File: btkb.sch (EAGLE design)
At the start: 1 part

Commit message: I added the RN-42 to the schematic! lol!
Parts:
- removed JP1: (no value), jumper:JP4E
- added U$1: BLUETOOTH-RN41", SparkFun-RF:BLUETOOTH-RN41"
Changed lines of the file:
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@@
 <layer number="48" name="Document" color="7" fill="1" visible="no" active="no"/>
 <layer number="49" name="Reference" color="7" fill="1" visible="no" active="no"/>
+<layer number="50" name="dxf" color="7" fill="1" visible="no" active="no"/>
 <layer number="51" name="tDocu" color="7" fill="1" visible="no" active="no"/>
 <layer number="52" name="bDocu" color="7" fill="1" visible="no" active="no"/>
+<layer number="53" name="tGND_GNDA" color="7" fill="9" visible="no" active="no"/>
+<layer number="54" name="bGND_GNDA" color="1" fill="9" visible="no" active="no"/>
+<layer number="56" name="wert" color="7" fill="1" visible="no" active="no"/>
+<layer number="57" name="tCAD" color="7" fill="1" visible="no" active="no"/>
 <layer number="90" name="Modules" color="5" fill="1" visible="yes" active="yes"/>
 <layer number="91" name="Nets" color="2" fill="1" visible="yes" active="yes"/>
@@
 <layer number="97" name="Info" color="7" fill="1" visible="yes" active="yes"/>
 <layer number="98" name="Guide" color="6" fill="1" visible="yes" active="yes"/>
+<layer number="99" name="SpiceOrder" color="7" fill="1" visible="no" active="no"/>
+<layer number="100" name="Muster" color="7" fill="1" visible="no" active="no"/>
+<layer number="101" name="Patch_Top" color="12" fill="4" visible="yes" active="yes"/>
+<layer number="102" name="Vscore" color="7" fill="1" visible="yes" active="yes"/>
+<layer number="103" name="tMap" color="7" fill="1" visible="yes" active="yes"/>
+<layer number="104" name="Name" color="16" fill="1" visible="yes" active="yes"/>
+<layer number="105" name="tPlate" color="7" fill="1" visible="yes" active="yes"/>
+<layer number="106" name="bPlate" color="7" fill="1" visible="yes" active="yes"/>
+<layer number="107" name="Crop" color="7" fill="1" visible="yes" active="yes"/>
+<layer number="108" name="tplace-old" color="10" fill="1" visible="yes" active="yes"/>
+<layer number="109" name="ref-old" color="11" fill="1" visible="yes" active="yes"/>
+<layer number="110" name="fp0" color="7" fill="1" visible="yes" active="yes"/>
+<layer number="111" name="LPC17xx" color="7" fill="1" visible="yes" active="yes"/>
+<layer number="112" name="tSilk" color="7" fill="1" visible="yes" active="yes"/>
+<layer number="113" name="IDFDebug" color="4" fill="1" visible="yes" active="yes"/>
+<layer number="116" name="Patch_BOT" color="9" fill="4" visible="yes" active="yes"/>
+<layer number="121" name="_tsilk" color="7" fill="1" visible="yes" active="yes"/>
+<layer number="122" name="_bsilk" color="7" fill="1" visible="yes" active="yes"/>
+<layer number="123" name="tTestmark" color="7" fill="1" visible="yes" active="yes"/>
+<layer number="124" name="bTestmark" color="7" fill="1" visible="yes" active="yes"/>
+<layer number="125" name="_tNames" color="7" fill="1" visible="yes" active="yes"/>
+<layer number="126" name="_bNames" color="7" fill="1" visible="yes" active="yes"/>
+<layer number="127" name="_tValues" color="7" fill="1" visible="yes" active="yes"/>
+<layer number="128" name="_bValues" color="7" fill="1" visible="yes" active="yes"/>
+<layer number="131" name="tAdjust" color="7" fill="1" visible="yes" active="yes"/>
+<layer number="132" name="bAdjust" color="7" fill="1" visible="yes" active="yes"/>
+<layer number="144" name="Drill_legend" color="7" fill="1" visible="yes" active="yes"/>
+<layer number="150" name="Notes" color="7" fill="1" visible="yes" active="yes"/>
+<layer number="151" name="HeatSink" color="7" fill="1" visible="yes" active="yes"/>
+<layer number="152" name="_bDocu" color="7" fill="1" visible="yes" active="yes"/>
+<layer number="153" name="FabDoc1" color="7" fill="1" visible="yes" active="yes"/>
+<layer number="154" name="FabDoc2" color="7" fill="1" visible="yes" active="yes"/>
+<layer number="155" name="FabDoc3" color="7" fill="1" visible="yes" active="yes"/>
+<layer number="199" name="Contour" color="7" fill="1" visible="yes" active="yes"/>
+<layer number="200" name="200bmp" color="1" fill="10" visible="yes" active="yes"/>
+<layer number="201" name="201bmp" color="2" fill="10" visible="yes" active="yes"/>
+<layer number="202" name="202bmp" color="3" fill="10" visible="yes" active="yes"/>
+<layer number="203" name="203bmp" color="4" fill="10" visible="yes" active="yes"/>
+<layer number="204" name="204bmp" color="5" fill="10" visible="yes" active="yes"/>
+<layer number="205" name="205bmp" color="6" fill="10" visible="yes" active="yes"/>
+<layer number="206" name="206bmp" color="7" fill="10" visible="yes" active="yes"/>
+<layer number="207" name="207bmp" color="8" fill="10" visible="yes" active="yes"/>
+<layer number="208" name="208bmp" color="9" fill="10" visible="yes" active="yes"/>
+<layer number="209" name="209bmp" color="7" fill="1" visible="yes" active="yes"/>
+<layer number="210" name="210bmp" color="7" fill="1" visible="yes" active="yes"/>
+<layer number="211" name="211bmp" color="7" fill="1" visible="yes" active="yes"/>
+<layer number="212" name="212bmp" color="7" fill="1" visible="yes" active="yes"/>
+<layer number="213" name="213bmp" color="7" fill="1" visible="yes" active="yes"/>
+<layer number="214" name="214bmp" color="7" fill="1" visible="yes" active="yes"/>
+<layer number="215" name="215bmp" color="7" fill="1" visible="yes" active="yes"/>
+<layer number="216" name="216bmp" color="7" fill="1" visible="yes" active="yes"/>
+<layer number="217" name="217bmp" color="18" fill="1" visible="no" active="no"/>
+<layer number="218" name="218bmp" color="19" fill="1" visible="no" active="no"/>
+<layer number="219" name="219bmp" color="20" fill="1" visible="no" active="no"/>
+<layer number="220" name="220bmp" color="21" fill="1" visible="no" active="no"/>
+<layer number="221" name="221bmp" color="22" fill="1" visible="no" active="no"/>
+<layer number="222" name="222bmp" color="23" fill="1" visible="no" active="no"/>
+<layer number="223" name="223bmp" color="24" fill="1" visible="no" active="no"/>
+<layer number="224" name="224bmp" color="25" fill="1" visible="no" active="no"/>
+<layer number="248" name="Housing" color="7" fill="1" visible="yes" active="yes"/>
+<layer number="249" name="Edge" color="7" fill="1" visible="yes" active="yes"/>
+<layer number="250" name="Descript" color="3" fill="1" visible="no" active="no"/>
+<layer number="251" name="SMDround" color="12" fill="11" visible="no" active="no"/>
+<layer number="254" name="cooling" color="7" fill="1" visible="yes" active="yes"/>
 </layers>
 <schematic xreflabel="%F%N/%S.%C%R" xrefpart="/%S.%C%R">
@@
 </classes>
 <parts>
-<part name="JP1" library="jumper" deviceset="JP4E" device=""/>
+<part name="U$1" library="SparkFun-RF" deviceset="BLUETOOTH-RN41" device="&quot;"/>
 </parts>
 <sheets>
@@
 </plain>
 <instances>
-<instance part="JP1" gate="G$1" x="20.32" y="93.98"/>
+<instance part="U$1" gate="G$1" x="73.66" y="12.7"/>
 </instances>
 <busses>

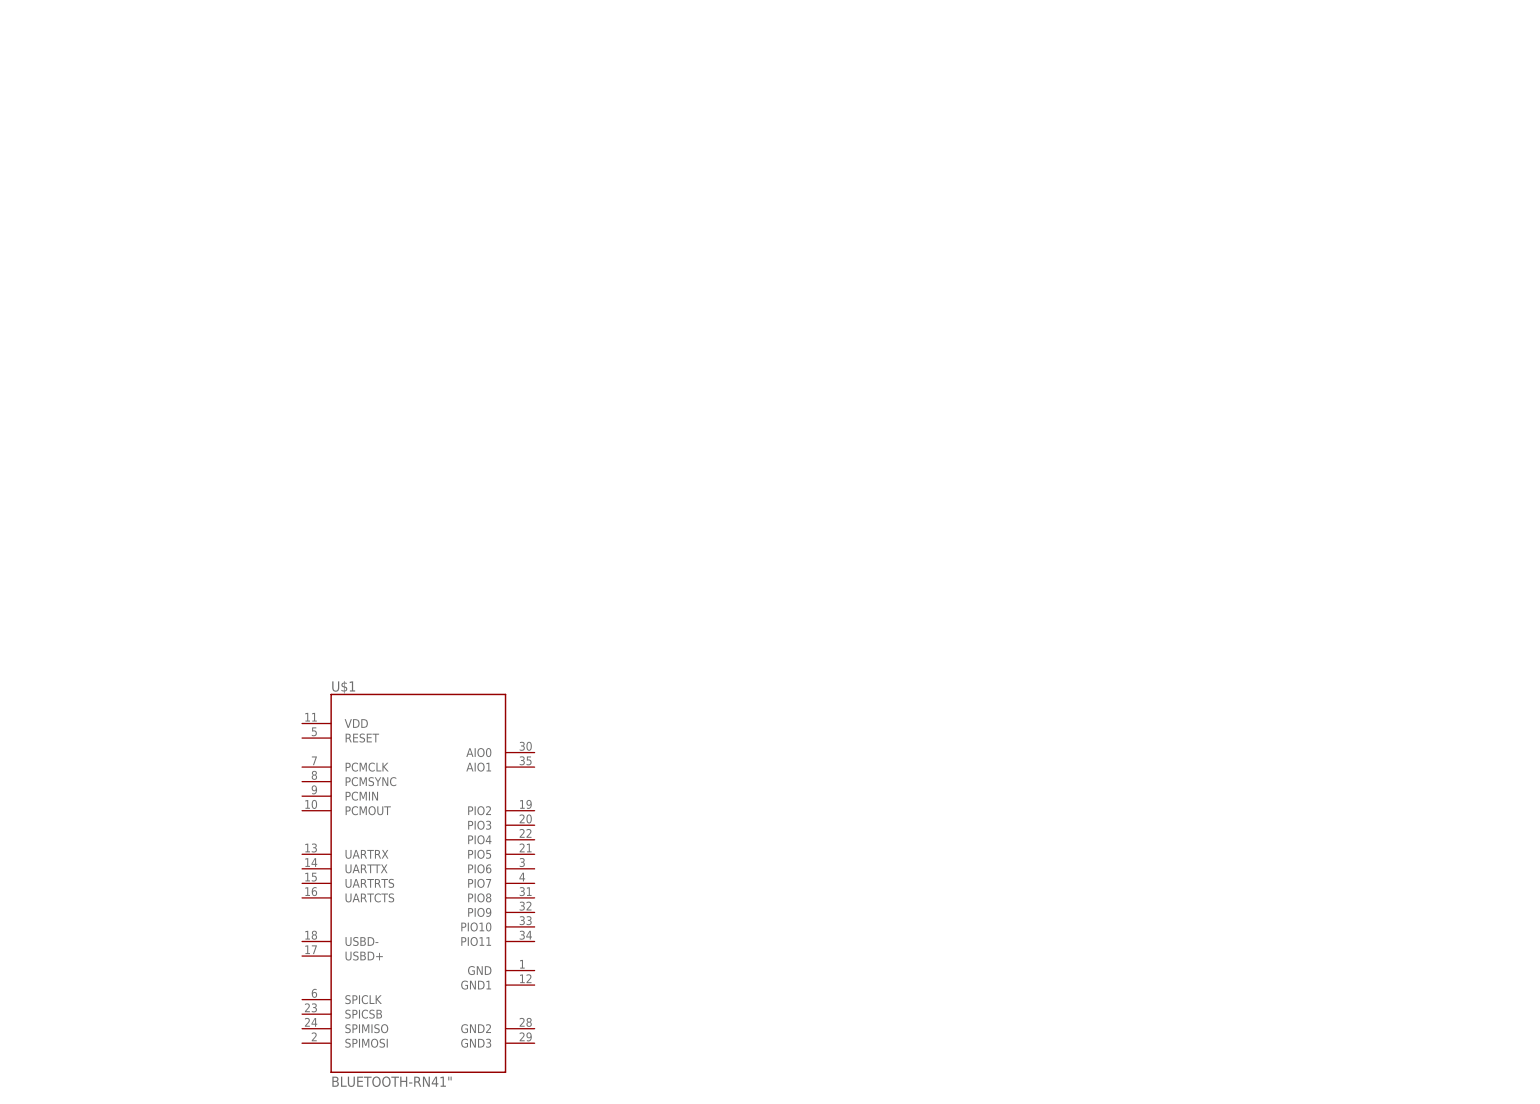
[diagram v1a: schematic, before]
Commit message: Added components copy pasta'ed from other schematics
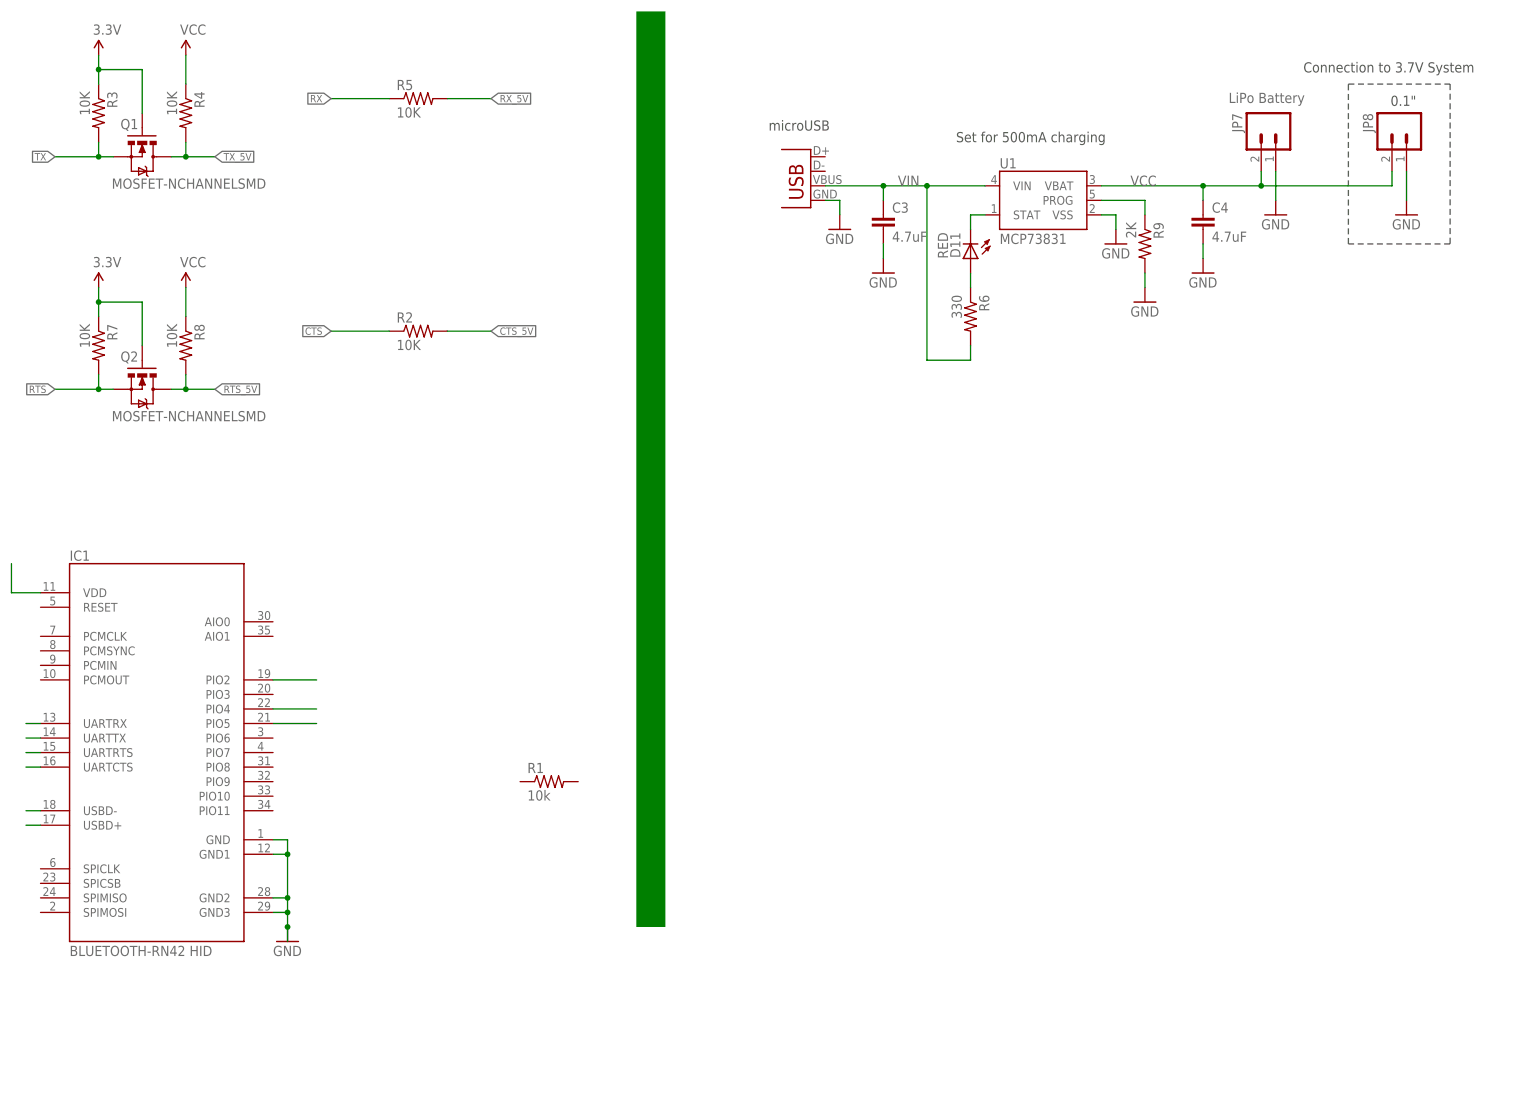
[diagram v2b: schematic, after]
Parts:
- removed U$1: BLUETOOTH-RN41", SparkFun-RF:BLUETOOTH-RN41"
- added C3, C4: 4.7uF, SparkFun:CAP0402-CAP
- added D11: RED, SparkFun:LED0603
- added IC1: BLUETOOTH-RN42 HID, SparkFun-RF:BLUETOOTH-RN41"
- added JP7: LiPo Battery, SparkFun:M02-JST-2MM-SMT
- added JP8: (no value), SparkFun:M02PTH
- added Q1, Q2: MOSFET-NCHANNELSMD, SparkFun:MOSFET-NCHANNELSMD
- added R1: 10k, SparkFun-Resistors:0.22OHM-1/4W-1%(0805)
- added R2, R3, R4, R5, R7, R8: 10K, SparkFun:RESISTOR0603-RES
- added R6: 330, SparkFun:RESISTOR0402-RES
- added R9: 2K, SparkFun:RESISTOR0402-RES
- added U1: MCP73831, SparkFun:MCP73831
- added X1: Micro USB, SparkFun:USB-MICROB
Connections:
- new net 3.3V: Q1.G, Q2.G, R3.1, R7.1
- new net CTS: R2.1
- new net CTS_5V: R2.2
- new net GND: C3.2, C4.2, IC1.GND, IC1.GND1, IC1.GND2, IC1.GND3, JP7.1, JP8.1, R9.2, U1.VSS, X1.GND
- new net N$1: IC1.UARTRX
- new net N$10: IC1.PIO5
- new net N$11: IC1.VDD
- new net N$12: D11.A, R6.1
- new net N$2: IC1.UARTTX
- new net N$3: IC1.UARTRTS
- new net N$4: IC1.UARTCTS
- new net N$5: IC1.USBD-
- new net N$6: IC1.USBD+
- new net N$8: IC1.PIO2
- new net N$9: IC1.PIO4
- new net PROG: R9.1, U1.PROG
- new net RTS: Q2.S, R7.2
- new net RTS_5V: Q2.D, R8.2
- new net RX: R5.1
- new net RX_5V: R5.2
- new net STAT: D11.C, U1.STAT
- new net TX: Q1.S, R3.2
- new net TX_5V: Q1.D, R4.2
- new net VCC: C4.1, JP7.2, JP8.2, R4.1, R8.1, U1.VBAT
- new net VIN: C3.1, R6.2, U1.VIN, X1.VBUS
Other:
- note added: "0.1""
- note added: "Connection to 3.7V System"
- note added: "Set for 500mA charging"
- note added: "microUSB"
